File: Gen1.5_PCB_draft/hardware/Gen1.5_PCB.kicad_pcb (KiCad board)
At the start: 4 copper layers, 74.8 x 101.5 mm, 67 parts, among them IC1 TJA1050T, J1 Enc1, J10 jumper2, J11 jumper4, J12 Enc2, J13 Enc3, J14 Enc4, J15 Enc5, J16 Enc6, J17 UART/CAN, J2 Booster, J4 UART/CAN, J5 MCP1, J6 MCP2, J7 MCP3, J8 UART/CAN, J9 jumper5, P2 LC1, P3 LC2, P4 LC3, P5 LC4, U1 ESP32-P4-ETH, U10 INA118U_2K5, U11 INA118U_2K5, U12 INA118U_2K5, U2 4754, U4 REF2033QDDCRQ1, U8 level shifter, U9 INA118U_2K5

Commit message: fixed pcb
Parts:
- removed J1: Enc1, Gen1.5_PCB:molex_5pin
- removed J10: jumper2, Gen1.5_PCB:CONN_3pin_jumper
- removed J11: jumper4, Gen1.5_PCB:CONN_3pin_jumper
- removed J17, J4, J8: UART/CAN, Gen1.5_PCB:CONN_3pin_jumper
- removed J9: jumper5, Gen1.5_PCB:CONN_3pin_jumper
- added C21: 68nF, Gen1.5_PCB:CAP_68nF, F.Cu at (140.5, 115.7)
- added C22: 6.8nF, Gen1.5_PCB:CAP_6.8nF, F.Cu at (137.8, 117.2)
- added C23: 6.8nF, Gen1.5_PCB:CAP_6.8nF, F.Cu at (137.8, 113.5)
- added C24: 6.8nF, Gen1.5_PCB:CAP_6.8nF, F.Cu at (138.1, 108.2)
- added C25: 68nF, Gen1.5_PCB:CAP_68nF, F.Cu at (140.7, 106.3)
- added C26: 6.8nF, Gen1.5_PCB:CAP_6.8nF, F.Cu at (138.1, 104.4)
- added C27: 6.8nF, Gen1.5_PCB:CAP_6.8nF, F.Cu at (138.3, 99.3)
- added C28: 68nF, Gen1.5_PCB:CAP_6.8nF, F.Cu at (140.9, 97.2)
- added C29: 6.8nF, Gen1.5_PCB:CAP_6.8nF, F.Cu at (138.3, 95.4)
- added C30: 6.8nF, Gen1.5_PCB:CAP_6.8nF, F.Cu at (138.3, 90.8)
- added C31: 68nF, Gen1.5_PCB:CAP_68nF, F.Cu at (141.1, 88.9)
- added C32: 6.8nF, Gen1.5_PCB:CAP_6.8nF, F.Cu at (138.3, 87.1)
- added C33: 47nF, Gen1.5_PCB:CAP_47nF, F.Cu at (191.2, 98.7)
- added C34: 8.2nF, Gen1.5_PCB:CAP_8.2nF, F.Cu at (130.6, 47.2)
- added J3: Enc1, Gen1.5_PCB:molex_5pin, F.Cu at (149.7, 70.7)
- added R17: 5k, Gen1.5_PCB:RES_5k, F.Cu at (134.6, 95.9)
- added R18: 10, Gen1.5_PCB:RES_10, F.Cu at (132.0, 43.7)
- added R19: 5k, Gen1.5_PCB:RES_5k, F.Cu at (134.7, 87.5)
- added R21: 60, Gen1.5_PCB:RES_60, F.Cu at (196.5, 103.9)
- added R22: 60, Gen1.5_PCB:RES_60, F.Cu at (185.8, 98.9)
- added R23: 60, Gen1.5_PCB:RES_60, F.Cu at (196.5, 98.9)
- added S1: EN termination low, Gen1.5_PCB:switch, F.Cu at (185.2, 93.6)
- added S2: EN loopback low, Gen1.5_PCB:switch, F.Cu at (185.2, 109.8)
- added S3: EN termination high, Gen1.5_PCB:switch, F.Cu at (196.9, 93.6)
- added S4: EN loopback high, Gen1.5_PCB:switch, F.Cu at (197.0, 109.8)
- added S5: jumper1, Gen1.5_PCB:switch, F.Cu at (184.8, 62.4)
- added S6: jumper2, Gen1.5_PCB:switch, F.Cu at (184.8, 67.8)
- C10, C13, C16, C6, C8, U4: moved to F.Cu
- C12, C5, C9: value 0.1uf -> 8.2nF; footprint Gen1.5_PCB:CAP_0.1uF_50V -> Gen1.5_PCB:CAP_8.2nF; moved to F.Cu
- C15: value 0.1uf -> 47nF; footprint Gen1.5_PCB:CAP_0.1uF_50V -> Gen1.5_PCB:CAP_47nF; moved to F.Cu
- C2, C3: value 47nF -> 8.2nF; footprint Gen1.5_PCB:CAP_47nF -> Gen1.5_PCB:CAP_8.2nF
- J5: value MCP1 -> Roboclaw1
- J6: value MCP2 -> Roboclaw2
- J7: value MCP3 -> Roboclaw3
- P2: value LC1 -> loadcell 1
- P3: value LC2 -> loadcell 2
- P4: value LC3 -> loadcell 3
- P5: value LC4 -> loadcell 4
- R1, R2, R3: value 60 -> 10; footprint Gen1.5_PCB:RES_60 -> Gen1.5_PCB:RES_10
- R10, R7: value 500 -> 5k; footprint Gen1.5_PCB:RES_510 -> Gen1.5_PCB:RES_5k
- R11, R5, R8: value 33k -> 5k; footprint Gen1.5_PCB:RES_33k -> Gen1.5_PCB:RES_5k
- R12, R9: value 12k -> 931; footprint Gen1.5_PCB:RES_12k -> Gen1.5_PCB:RES_931
- R13, R4: value 500 -> 931; footprint Gen1.5_PCB:RES_510 -> Gen1.5_PCB:RES_931
- R14: value 33k -> 10; footprint Gen1.5_PCB:RES_33k -> Gen1.5_PCB:RES_10
- R15: value 12k -> 10; footprint Gen1.5_PCB:RES_12k -> Gen1.5_PCB:RES_10
- R6: value 12k -> 5k; footprint Gen1.5_PCB:RES_12k -> Gen1.5_PCB:RES_5k
- moved C9 80.7 mm to (130.6, 38.8), turned to 0 degrees
- moved C5 67.9 mm to (130.9, 63.9), turned to 0 degrees
- moved IC1 64.8 mm to (192.2, 86.4)
- moved C1 64.6 mm to (187.3, 87.5), turned to -90 degrees
- moved P2 63.8 mm to (120.9, 114.7), turned to 180 degrees
- moved P3 63.8 mm to (121.0, 105.9), turned to 180 degrees
- moved P4 63.7 mm to (121.0, 96.8), turned to 180 degrees
- moved P5 63.5 mm to (121.2, 88.1), turned to 180 degrees
- moved R14 60.7 mm to (132.1, 35.2)
- moved R2 58.2 mm to (131.9, 52.4), turned to 180 degrees
- moved C12 52.3 mm to (130.5, 79.7), turned to 0 degrees
- moved C3 50.0 mm to (130.4, 55.9), turned to 0 degrees
- moved R16 49.5 mm to (185.8, 103.9)
- moved U8 48.1 mm to (181.9, 86.5)
- moved C19 47.9 mm to (185.3, 86.2)
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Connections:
- C1 pad 1: /5V -> 5V
- C12 pad 1: /loadcells/Vin(-) 3 -> /MISO
- C12 pad 2: /loadcells/Vin(+) 3 -> GND
- C15 pad 1: /loadcells/Vin(-) 4 -> Net-(C15-Pad1)
- C15 pad 2: /loadcells/Vin(+) 4 -> GND
- C2 pad 1: GND -> /MISO
- C2 pad 2: Net-(C2-Pad2) -> GND
- C20 pad 1: /5V -> 5V
- C3 pad 1: GND -> /MISO
- C3 pad 2: Net-(C3-Pad2) -> GND
- C5 pad 1: /loadcells/Vin(-) 1 -> /MISO
- C5 pad 2: /loadcells/Vin(+) 1 -> GND
- C8 pad 2: /loadcells/5V -> 5V
- C9 pad 1: /loadcells/Vin(-) 2 -> /MISO
- C9 pad 2: /loadcells/Vin(+) 2 -> GND
- FB2 pad 1: /5V -> 5V
- IC1 pad 3: /5V -> 5V
- J12 pad 1: /3V3 -> GND
- J12 pad 2: /MISO -> /CS2
- J12 pad 3: /CLK -> /3V3
- J12 pad 4: /CS2 -> /CLK
- J12 pad 5: GND -> Net-(J12-Pin_5)
- J13 pad 1: /3V3 -> GND
- J13 pad 2: /MISO -> /CS4
- J13 pad 3: /CLK -> /3V3
- J13 pad 4: /CS4 -> /CLK
- J13 pad 5: GND -> Net-(J13-Pin_5)
- J14 pad 1: /3V3 -> GND
- J14 pad 2: /MISO -> /CS6
- J14 pad 3: /CLK -> /3V3
- J14 pad 4: /CS6 -> /CLK
- J14 pad 5: GND -> Net-(J14-Pin_5)
- J15 pad 1: /3V3 -> GND
- J15 pad 2: /MISO -> /CS1
- J15 pad 3: /CLK -> /3V3
- J15 pad 4: /CS1 -> /CLK
- J15 pad 5: GND -> Net-(J15-Pin_5)
- J16 pad 1: /3V3 -> GND
- J16 pad 2: /MISO -> /CS3
- J16 pad 3: /CLK -> /3V3
- J16 pad 4: /CS3 -> /CLK
- J16 pad 5: GND -> Net-(J16-Pin_5)
- J2 pad 3: /5V -> 5V
- J6 pad 2: Net-(J11-Pin_2) -> /TX2
- J6 pad 3: Net-(J6-Pin_3) -> /RX2
- J7 pad 2: Net-(J17-Pin_2) -> /TX3
- J7 pad 3: Net-(J7-Pin_3) -> /RX3
- R1 pad 1: /CANH -> Net-(J3-Pin_5)
- R1 pad 2: Net-(C2-Pad2) -> /MISO
- R10 pad 1: Net-(U11-RG__1) -> /loadcells/Vin(+) 3
- R10 pad 2: Net-(U11-RG) -> Net-(U11-V+_IN)
- R11 pad 1: /loadcells/INAout 3 -> /loadcells/Vin(+) 4
- R11 pad 2: LC3 -> Net-(U12-V+_IN)
- R12 pad 1: GND -> Net-(U11-RG__1)
- R12 pad 2: LC3 -> Net-(U11-RG)
- R14 pad 1: /loadcells/INAout 4 -> Net-(J13-Pin_5)
- R14 pad 2: LC4 -> /MISO
- R15 pad 1: GND -> Net-(J14-Pin_5)
- R15 pad 2: LC4 -> /MISO
- R16 pad 1: Net-(C3-Pad2) -> /LL
- R16 pad 2: /CANL -> Net-(C15-Pad1)
- R2 pad 1: Net-(C2-Pad2) -> Net-(J12-Pin_5)
- R2 pad 2: /CANL -> /MISO
- R3 pad 1: /CANH -> Net-(J15-Pin_5)
- R3 pad 2: Net-(C3-Pad2) -> /MISO
- R5 pad 1: /loadcells/INAout 1 -> /loadcells/Vin(+) 1
- R5 pad 2: LC1 -> Net-(U9-V+_IN)
- R6 pad 1: GND -> /loadcells/Vin(-) 1
- R6 pad 2: LC1 -> Net-(U9-V-_IN)
- R7 pad 1: Net-(U10-RG__1) -> /loadcells/Vin(+) 2
- R7 pad 2: Net-(U10-RG) -> Net-(U10-V+_IN)
- R8 pad 1: /loadcells/INAout 2 -> /loadcells/Vin(-) 2
- R8 pad 2: LC2 -> Net-(U10-V-_IN)
- R9 pad 1: GND -> Net-(U10-RG__1)
- R9 pad 2: LC2 -> Net-(U10-RG)
- U10 pad 2: /loadcells/Vin(-) 2 -> Net-(U10-V-_IN)
- U10 pad 3: /loadcells/Vin(+) 2 -> Net-(U10-V+_IN)
- U10 pad 6: /loadcells/INAout 2 -> LC2
- U11 pad 2: /loadcells/Vin(-) 3 -> Net-(U11-V-_IN)
- U11 pad 3: /loadcells/Vin(+) 3 -> Net-(U11-V+_IN)
- U11 pad 6: /loadcells/INAout 3 -> LC3
- U12 pad 2: /loadcells/Vin(-) 4 -> Net-(U12-V-_IN)
- U12 pad 3: /loadcells/Vin(+) 4 -> Net-(U12-V+_IN)
- U12 pad 6: /loadcells/INAout 4 -> LC4
- U4 pad 3: /loadcells/5V -> 5V
- U4 pad 4: /loadcells/5V -> 5V
- U9 pad 2: /loadcells/Vin(-) 1 -> Net-(U9-V-_IN)
- U9 pad 3: /loadcells/Vin(+) 1 -> Net-(U9-V+_IN)
- U9 pad 6: /loadcells/INAout 1 -> LC1
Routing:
- net /CANL: track 101.1 -> 0.00 mm, vias 1 -> 0
- net /CANH: track 100.9 -> 0.00 mm, vias 1 -> 0
- net /CAN TX: track 66.5 -> 0.00 mm, vias 1 -> 0
- net 10V: track 140.5 -> 85.1 mm, vias 0 -> 4
- net /5V: track 51.6 -> 0.00 mm, vias 1 -> 0
- net /CS5: track 30.3 -> 75.9 mm
- net 5V: track 0.00 -> 40.0 mm, vias 0 -> 1
- net /SDA: track 39.5 -> 0.00 mm
- net /SCL: track 30.0 -> 0.00 mm
- net /CAN RX_1: track 28.8 -> 0.00 mm, vias 1 -> 0
- net /CS6: track 41.4 -> 68.6 mm
- net /TX1: track 24.2 -> 0.00 mm
- net /RX1: track 24.0 -> 0.00 mm
- net /TX3: track 23.9 -> 0.00 mm, vias 1 -> 0
- net /RX2: track 23.5 -> 0.00 mm
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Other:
- board size 74.8 x 101.5 mm -> 93.8 x 109.2 mm

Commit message: labeling and aligning
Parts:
- added REF**: MountingHole_3.97mm, MountingHole:MountingHole_4mm, F.Cu at (210.9, 132.4)
- added REF**: MountingHole_3.97mm, MountingHole:MountingHole_4mm, F.Cu at (210.9, 34.5)
- added REF**: MountingHole_3.97mm, MountingHole:MountingHole_4mm, F.Cu at (113.6, 132.4)
- added REF**: MountingHole_3.97mm, MountingHole:MountingHole_4mm, F.Cu at (113.6, 34.5)
- added kibuzzard-6A8859E8: G***, kibuzzard-6A8859E8, F.Cu at (205.2, 61.8)
- added kibuzzard-6A8859F9: G***, kibuzzard-6A8859F9, F.Cu at (205.2, 79.0)
- added kibuzzard-6A885A00: G***, kibuzzard-6A885A00, F.Cu at (205.2, 70.4)
- added kibuzzard-6A885C51: G***, kibuzzard-6A885C51, F.Cu at (124.8, 68.7)
- added kibuzzard-6A885C51: G***, kibuzzard-6A885C51, F.Cu at (124.8, 35.1)
- added kibuzzard-6A885C51: G***, kibuzzard-6A885C51, F.Cu at (124.8, 76.2)
- added kibuzzard-6A885C51: G***, kibuzzard-6A885C51, F.Cu at (124.8, 52.4)
- added kibuzzard-6A885C51: G***, kibuzzard-6A885C51, F.Cu at (124.8, 60.4)
- added kibuzzard-6A885C51: G***, kibuzzard-6A885C51, F.Cu at (124.8, 43.8)
- added kibuzzard-6A885C67: G***, kibuzzard-6A885C67, F.Cu at (198.9, 92.9)
- added kibuzzard-6A885C67: G***, kibuzzard-6A885C67, F.Cu at (186.6, 92.8)
- added kibuzzard-6A885C86: G***, kibuzzard-6A885C86, F.Cu at (198.7, 104.3)
- added kibuzzard-6A885C86: G***, kibuzzard-6A885C86, F.Cu at (186.8, 104.3)
- C1, C19, IC1, U8: moved to B.Cu
- moved C15 8.93 mm to (192.7, 112.6)
- moved R21 8.83 mm to (198.1, 112.6)
- moved R16 8.81 mm to (187.2, 112.6)
- moved IC1 7.09 mm to (185.6, 88.9)
- moved C1 6.57 mm to (180.9, 88.8)
- moved U8 4.05 mm to (184.0, 83.0)
- moved S3 3.11 mm to (198.8, 96.1)
- moved C19 3.01 mm to (187.1, 83.8), turned to -90 degrees
- moved C33 2.96 mm to (192.7, 101.3)
- moved S1 2.75 mm to (186.5, 96.0)
- moved S4 2.71 mm to (198.8, 107.7)
- moved R23 2.61 mm to (198.1, 101.0)
- moved S2 2.51 mm to (186.4, 107.6)
- moved R22 2.50 mm to (187.2, 101.0)
- moved U2 1.80 mm to (192.2, 42.8)
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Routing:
- net /3V3: track 152.8 -> 212.6 mm, vias 0 -> 2
- net 5V: track 40.0 -> 90.2 mm, vias 1 -> 2
- net /CANH: track 0.00 -> 45.2 mm
- net 10V: track 85.1 -> 119.0 mm
- net /CANL: track 0.00 -> 31.5 mm
- net /TX3: track 0.00 -> 29.3 mm
- net /RX2: track 0.00 -> 28.6 mm
- net /RX3: track 0.00 -> 28.6 mm
- net /TX2: track 0.00 -> 25.8 mm
- net /SCL: track 0.00 -> 25.2 mm
- net /SDA: track 0.00 -> 20.2 mm
- net /TH: track 0.00 -> 18.1 mm
- net /CAN RX_1: track 0.00 -> 18.0 mm
- net /TL: track 0.00 -> 16.8 mm
- net Net-(J5-Pin_3): track 0.00 -> 16.8 mm
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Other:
- board size 93.8 x 109.2 mm -> 110.2 x 109.2 mm

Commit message: added test points
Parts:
- removed the kibuzzard-6A885C51 at (124.8, 68.7)
- removed the kibuzzard-6A885C51 at (124.8, 76.2)
- removed the kibuzzard-6A885C51 at (124.8, 52.4)
- removed the kibuzzard-6A885C51 at (124.8, 60.4)
- removed the kibuzzard-6A885C51 at (124.8, 43.8)
- added kibuzzard-6A88605B: G***, kibuzzard-6A88605B, F.Cu at (124.8, 44.9)
- added kibuzzard-6A886062: G***, kibuzzard-6A886062, F.Cu at (124.8, 53.1)
- added kibuzzard-6A886067: G***, kibuzzard-6A886067, F.Cu at (124.8, 61.3)
- added kibuzzard-6A88606D: G***, kibuzzard-6A88606D, F.Cu at (124.8, 69.5)
- added kibuzzard-6A886074: G***, kibuzzard-6A886074, F.Cu at (124.8, 77.6)
- added kibuzzard-6A8860CE: G***, kibuzzard-6A8860CE, F.Cu at (184.8, 58.4)
- added kibuzzard-6A88645C: G***, kibuzzard-6A88645C, F.Cu at (113.4, 114.8)
- added kibuzzard-6A886473: G***, kibuzzard-6A886473, F.Cu at (113.4, 106.1)
- added kibuzzard-6A88647E: G***, kibuzzard-6A88647E, F.Cu at (113.4, 88.9)
- added kibuzzard-6A886487: G***, kibuzzard-6A886487, F.Cu at (113.4, 97.3)
- added kibuzzard-6A886536: G***, kibuzzard-6A886536, F.Cu at (144.7, 31.9)
- added kibuzzard-6A886715: G***, kibuzzard-6A886715, F.Cu at (125.0, 84.1)
- added kibuzzard-6A8868AC: G***, kibuzzard-6A8868AC, F.Cu at (197.9, 83.9)
- added kibuzzard-6A8868D3: G***, kibuzzard-6A8868D3, F.Cu at (197.8, 57.0)
- C28: footprint Gen1.5_PCB:CAP_6.8nF -> Gen1.5_PCB:CAP_68nF
- J12: value Enc2 -> Enc3
- J13: value Enc3 -> Enc1
- J14: value Enc4 -> Enc6
- J15: value Enc5 -> Enc4
- J16: value Enc6 -> Enc2
- J3: value Enc1 -> Enc5
- moved kibuzzard-6A885C51 1.59 mm to (124.8, 36.7)
- moved C28 0.97 mm to (141.1, 98.2)
- moved C21 0.64 mm to (141.1, 115.7)
- moved C22 0.54 mm to (138.3, 117.2)
- moved C23 0.54 mm to (138.3, 113.5)
- moved R5 0.54 mm to (134.7, 116.8)
- moved U10 0.53 mm to (146.8, 106.3)
- moved R6 0.52 mm to (134.7, 113.6)
- moved C25 0.42 mm to (141.1, 106.3)
- moved R7 0.42 mm to (134.7, 107.7)
- moved R8 0.42 mm to (134.7, 104.8)
- moved C10 0.30 mm to (151.7, 106.7)
- moved C11 0.30 mm to (151.7, 109.0)
- moved C6 0.30 mm to (151.7, 115.9)
- moved C7 0.30 mm to (151.7, 118.2)
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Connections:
- P2 pad 3: /loadcells/Vin(+) 1 -> GND
- P2 pad 4: GND -> /loadcells/Vin(+) 1
- P3 pad 3: /loadcells/Vin(+) 2 -> GND
- P3 pad 4: GND -> /loadcells/Vin(+) 2
- P4 pad 3: /loadcells/Vin(+) 3 -> GND
- P4 pad 4: GND -> /loadcells/Vin(+) 3
- P5 pad 3: /loadcells/Vin(+) 4 -> GND
- P5 pad 4: GND -> /loadcells/Vin(+) 4
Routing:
- net /loadcells/Vin(+) 3: track 7.80 -> 5.10 mm
- net /loadcells/Vin(+) 4: track 7.78 -> 5.24 mm
- net /loadcells/Vin(+) 2: track 7.51 -> 5.18 mm
- net /loadcells/Vin(+) 1: track 7.53 -> 5.26 mm
- net 10V: track 119.0 -> 120.3 mm
- net Net-(U10-V-_IN): track 9.24 -> 8.59 mm

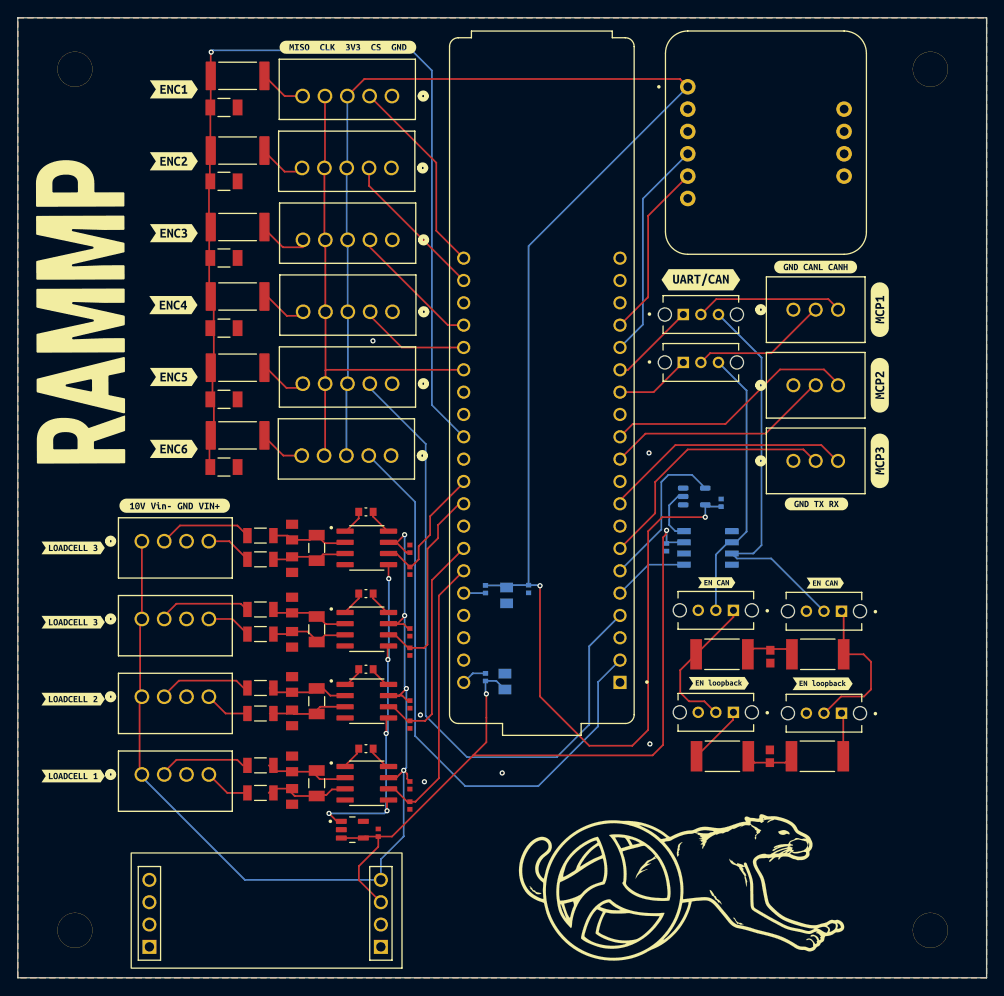
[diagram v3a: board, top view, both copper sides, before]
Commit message: added can test points
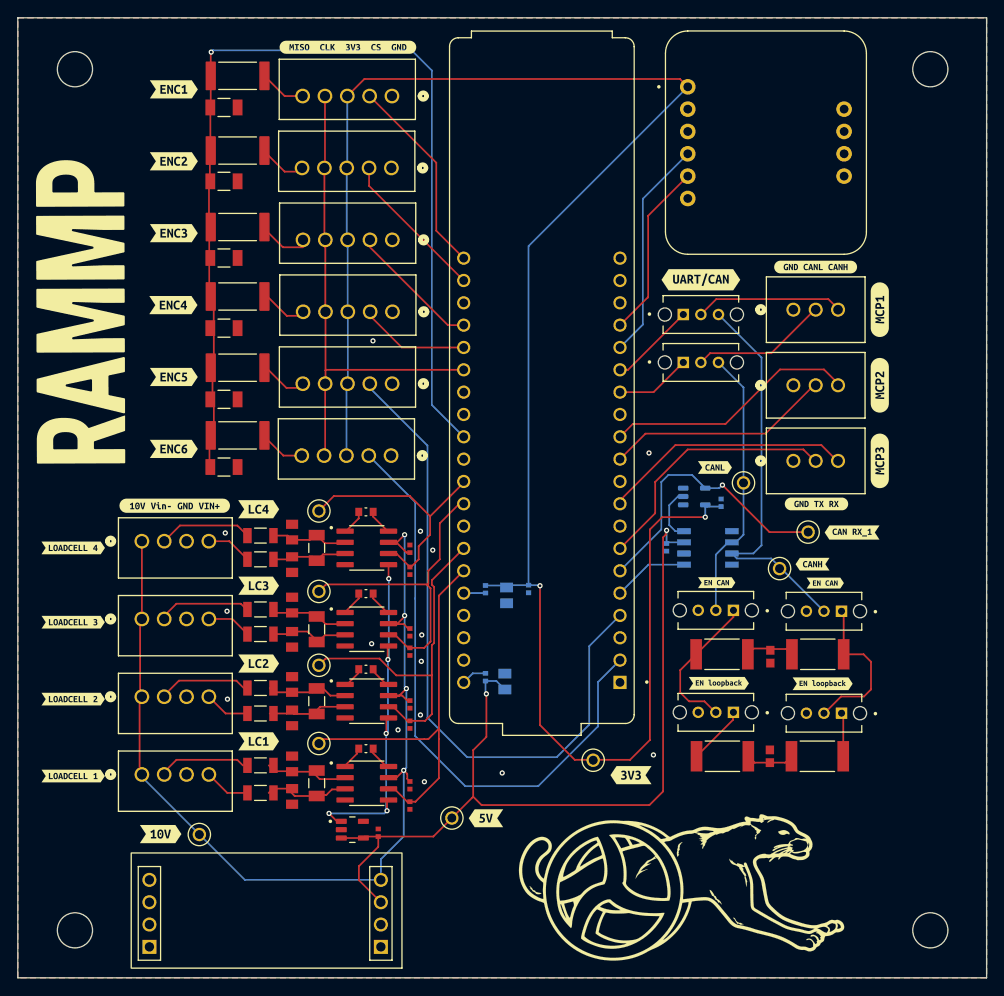
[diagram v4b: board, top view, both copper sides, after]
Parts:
- removed kibuzzard-6A88647E: G***, kibuzzard-6A88647E
- added TP1: 5003, Gen1.5_PCB:test_point, F.Cu at (141.3, 111.2)
- added TP10: 5003, Gen1.5_PCB:test_point, F.Cu at (197.0, 87.1)
- added TP2: 5003, Gen1.5_PCB:test_point, F.Cu at (141.3, 102.2)
- added TP3: 5003, Gen1.5_PCB:test_point, F.Cu at (141.3, 93.8)
- added TP4: 5003, Gen1.5_PCB:test_point, F.Cu at (141.3, 84.7)
- added TP5: 5003, Gen1.5_PCB:test_point, F.Cu at (172.6, 113.0)
- added TP6: 5003, Gen1.5_PCB:test_point, F.Cu at (156.5, 119.6)
- added TP7: 5003, Gen1.5_PCB:test_point, F.Cu at (127.8, 121.5)
- added TP8: 5003, Gen1.5_PCB:test_point, F.Cu at (189.7, 81.5)
- added TP9: 5003, Gen1.5_PCB:test_point, F.Cu at (193.8, 91.2)
- added kibuzzard-6A886B6D: G***, kibuzzard-6A886B6D, F.Cu at (123.3, 121.5)
- added kibuzzard-6A886D1F: G***, kibuzzard-6A886D1F, F.Cu at (160.3, 119.7)
- added kibuzzard-6A886D93: G***, kibuzzard-6A886D93, F.Cu at (176.8, 114.8)
- added kibuzzard-6A8871A1: G***, kibuzzard-6A8871A1, F.Cu at (113.4, 88.9)
- added kibuzzard-6A8871C3: G***, kibuzzard-6A8871C3, F.Cu at (134.5, 84.5)
- added kibuzzard-6A8871D7: G***, kibuzzard-6A8871D7, F.Cu at (134.5, 93.2)
- added kibuzzard-6A8871DC: G***, kibuzzard-6A8871DC, F.Cu at (134.5, 102.0)
- added kibuzzard-6A8871E1: G***, kibuzzard-6A8871E1, F.Cu at (134.5, 110.9)
- added kibuzzard-6A8884B3: G***, kibuzzard-6A8884B3, F.Cu at (186.4, 79.8)
- added kibuzzard-6A8884DE: G***, kibuzzard-6A8884DE, F.Cu at (197.5, 90.8)
- added kibuzzard-6A88850B: G***, kibuzzard-6A88850B, F.Cu at (202.0, 87.2)
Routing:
- net LC1: track 32.4 -> 46.7 mm
- net LC4: track 15.5 -> 29.8 mm
- net LC2: track 26.5 -> 40.7 mm
- net /CAN RX_1: track 18.0 -> 32.1 mm, vias 0 -> 1
- net LC3: track 23.4 -> 36.3 mm
- net 5V: track 90.2 -> 98.8 mm
- net /3V3: track 212.6 -> 216.6 mm
- net GND: vias 6 -> 15

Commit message: final changes before DR
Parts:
- added kibuzzard-6A8888D6: G***, kibuzzard-6A8888D6, F.Cu at (187.3, 36.5)
- added kibuzzard-6A8888E5: G***, kibuzzard-6A8888E5, F.Cu at (187.2, 41.5)
- added kibuzzard-6A888913: G***, kibuzzard-6A888913, F.Cu at (153.7, 126.7)
- added kibuzzard-6A888920: G***, kibuzzard-6A888920, F.Cu at (153.3, 129.1)
- added kibuzzard-6A88892B: G***, kibuzzard-6A88892B, F.Cu at (153.7, 131.6)
- added kibuzzard-6A8889CA: G***, kibuzzard-6A8889CA, F.Cu at (166.6, 46.1)

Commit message: finished mcp connector design
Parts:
- added R20: 5k, Gen1.5_PCB:RES_5k, B.Cu at (147.4, 67.5)
- added R24: 5k, Gen1.5_PCB:RES_5k, B.Cu at (147.4, 51.1)
- added R25: 5k, Gen1.5_PCB:RES_5k, B.Cu at (147.4, 34.8)
- added R26: 5k, Gen1.5_PCB:RES_5k, B.Cu at (147.4, 75.7)
- added R27: 5k, Gen1.5_PCB:RES_5k, B.Cu at (147.4, 59.3)
- added R28: 5k, Gen1.5_PCB:RES_5k, B.Cu at (147.4, 42.9)
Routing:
- net /3V3: track 216.6 -> 236.7 mm
- net /CS5: track 75.9 -> 79.5 mm
- net /CS3: track 16.8 -> 20.3 mm
- net /CS4: track 22.9 -> 26.4 mm
- net /CS6: track 68.6 -> 72.1 mm
- net /CS2: track 14.3 -> 17.7 mm
- net /CS1: track 12.1 -> 15.5 mm
- net GND: vias 15 -> 16
